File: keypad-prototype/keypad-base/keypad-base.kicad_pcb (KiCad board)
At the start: 2 copper layers, 150.2 x 64.2 mm, 66 parts, among them CON1 AVR-ISP-6, J1 USB_C_Receptacle_USB2.0, J2 Conn_01x02, J3 Conn_01x02, Q1 AO3400A, SW1 Switch_SW_Push, SW2 Switch_SW_Push, SW3 Switch_SW_Push, SW4 Switch_SW_Push, SW5 Switch_SW_Push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

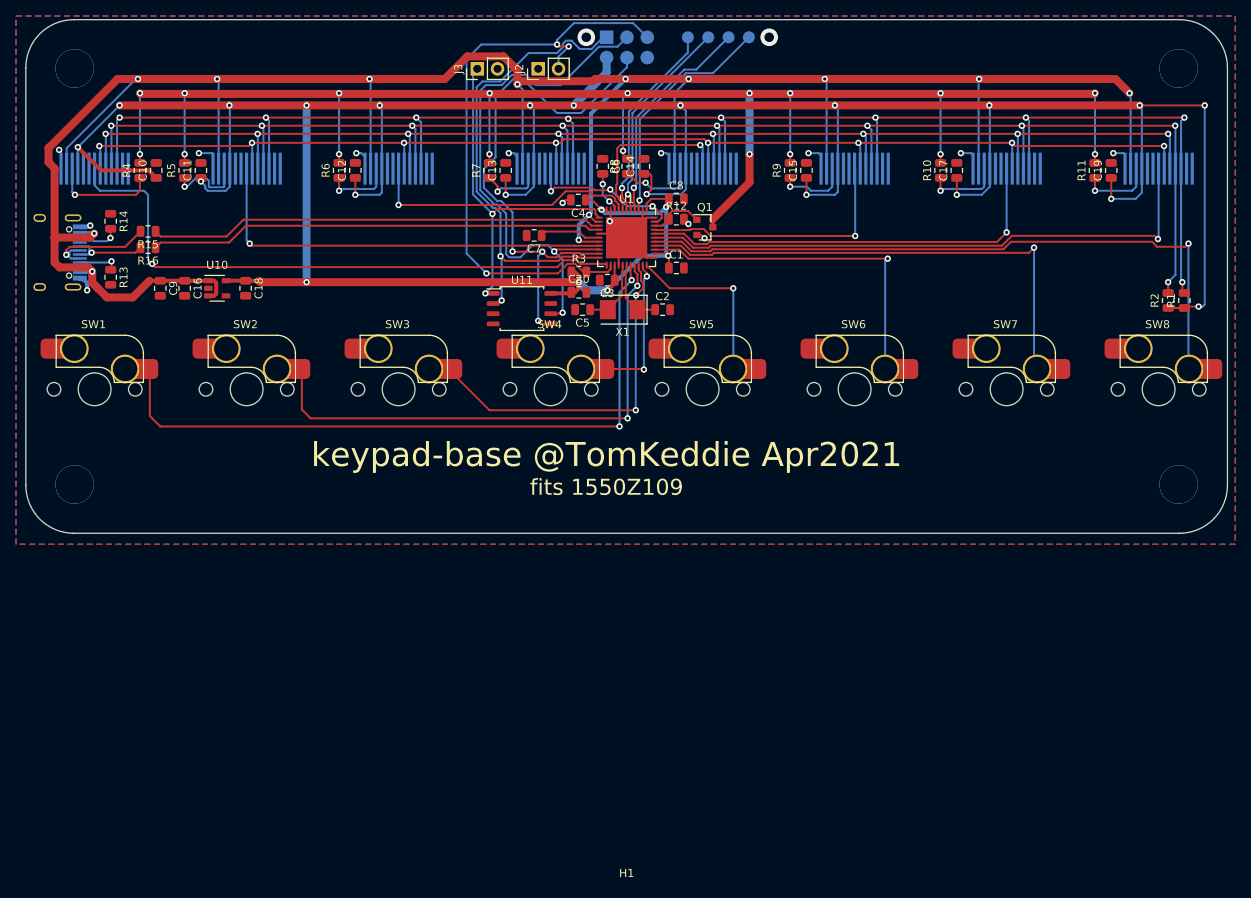
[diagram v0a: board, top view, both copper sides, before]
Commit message: keypad-base: reduced to 6 keys, add mode change side buttons
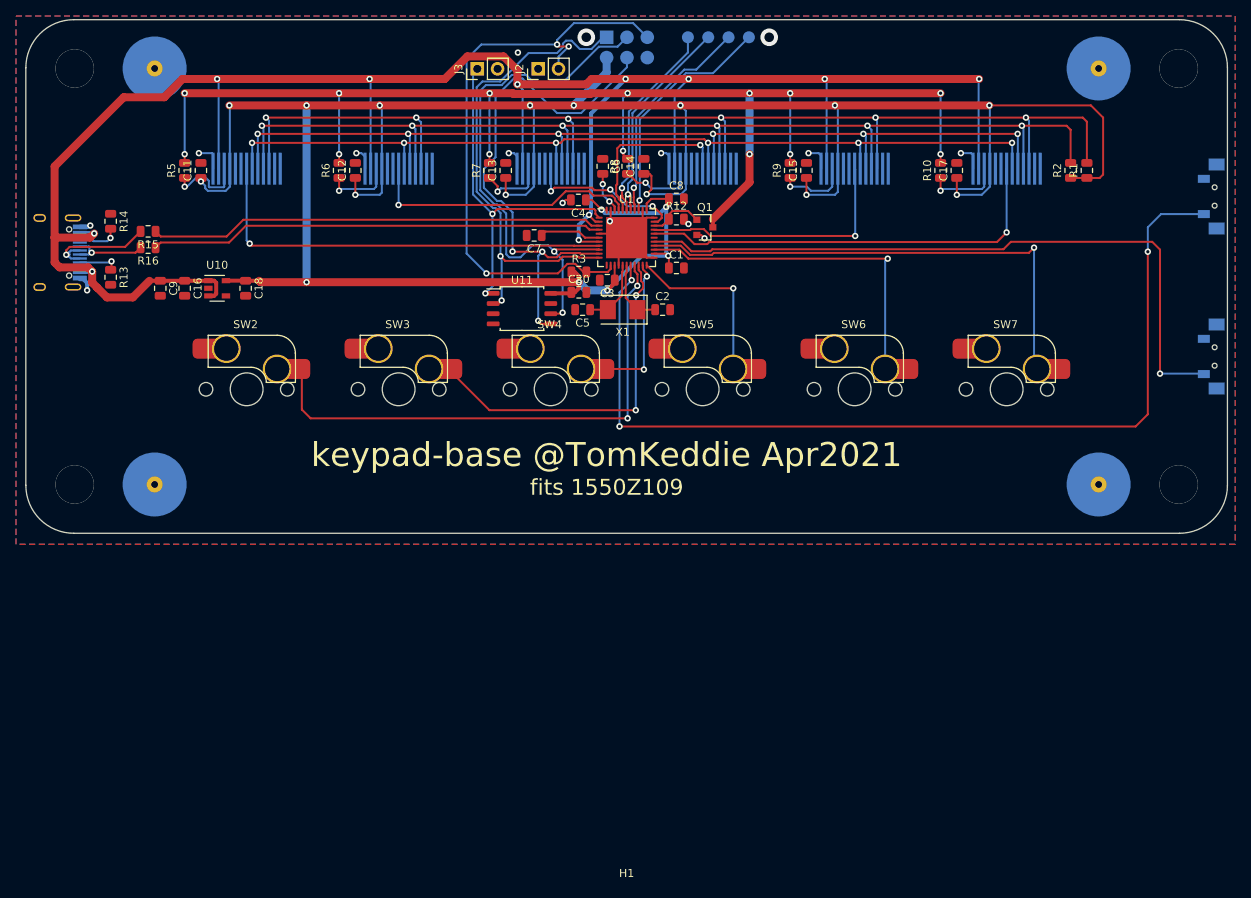
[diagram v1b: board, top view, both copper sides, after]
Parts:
- removed C10, C19: 0.1uF/6.3V, tom-passives:C_0805_2012Metric
- removed R11, R4: 470R, tom-passives:R_0805_2012Metric
- removed U2, U9: IE096HQ1301CL, tom-mechanical:IE096HQ1301CL
- added H2: mech-only-no-pins, tom-mechanical:STUD_SOLDER_M3, B.Cu at (225.5, 111.9)
- added H3: mech-only-no-pins, tom-mechanical:STUD_SOLDER_M3, B.Cu at (225.5, 59.9)
- added H4: mech-only-no-pins, tom-mechanical:STUD_SOLDER_M3, B.Cu at (107.5, 59.9)
- added H5: mech-only-no-pins, tom-mechanical:STUD_SOLDER_M3, B.Cu at (107.5, 111.9)
- SW1, SW8: footprint tom-mechanical:MX-KailhClip-1.00u-no-top-ring -> tom-mechanical:SW_SPST_SMD_SIDE_7.0x3.5; moved to B.Cu
- moved SW1 142.1 mm to (240.0, 75.9)
- moved R1 20.3 mm to (224.0, 72.6)
- moved R2 20.3 mm to (222.0, 72.6)
- moved SW8 8.11 mm to (240.0, 95.9)
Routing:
- net +3V3: track 429.8 -> 346.5 mm, vias 26 -> 20
- net /~CS1: track 75.7 -> 0.00 mm, vias 1 -> 0
- net /~CS8: track 73.1 -> 0.00 mm, vias 1 -> 0
- net /SCL: track 192.8 -> 138.6 mm, vias 9 -> 6
- net /SDA: track 201.3 -> 147.4 mm, vias 9 -> 6
- net /D\C: track 168.2 -> 121.6 mm, vias 8 -> 6
- net +5V: track 315.6 -> 269.1 mm, vias 13 -> 11
- net /~LCDRESET: track 159.0 -> 114.9 mm, vias 8 -> 6
- net /BACKLIGHTK: track 207.8 -> 165.5 mm, vias 18 -> 14
- net /SW1: track 89.1 -> 118.6 mm, vias 2 -> 3
- net Net-(R4-Pad1): track 13.3 -> 0.00 mm, vias 1 -> 0
- net GND: track 78.8 -> 68.2 mm, vias 16 -> 15
- net Net-(R11-Pad1): track 9.22 -> 0.00 mm, vias 1 -> 0
- net /SW8: track 86.3 -> 85.6 mm

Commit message: keypad-base: Apr2021 release
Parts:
- added R11: 10k, tom-passives:R_0805_2012Metric, F.Cu at (161.0, 92.5)
- added R4: 10k, tom-passives:R_0805_2012Metric, F.Cu at (145.8, 90.4)
- R13, R14: value 10k -> 5.1k
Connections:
- U1 pad 12: /~CS1 -> /D\C
- U1 pad 28: /~CS8 -> /~LCDRESET
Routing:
- net /D\C: track 121.6 -> 154.6 mm, vias 6 -> 8
- net /~LCDRESET: track 114.9 -> 141.6 mm, vias 6 -> 8
- net Net-(R11-Pad2): track 0.00 -> 11.4 mm
- net +3V3: track 346.5 -> 350.4 mm
- net Net-(R4-Pad2): track 0.00 -> 3.14 mm
- net /~RESET: track 75.4 -> 76.1 mm
